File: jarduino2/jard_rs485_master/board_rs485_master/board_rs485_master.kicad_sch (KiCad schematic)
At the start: 27 parts, among them J1 POWER_12V, J2 ON_OFF, J3 POWER_OYAS_12V, J4 BUS_OYAS, J5 Leds RGB, Q1 BPC_2N2222A, Q2 BPC_IPP034N03L, Q3 BC327, U1 RtcArduino, U2 BPC_Alim3_3V, U3 BPC_ATMEGA2560_PRO, U4 BPC_Mod485

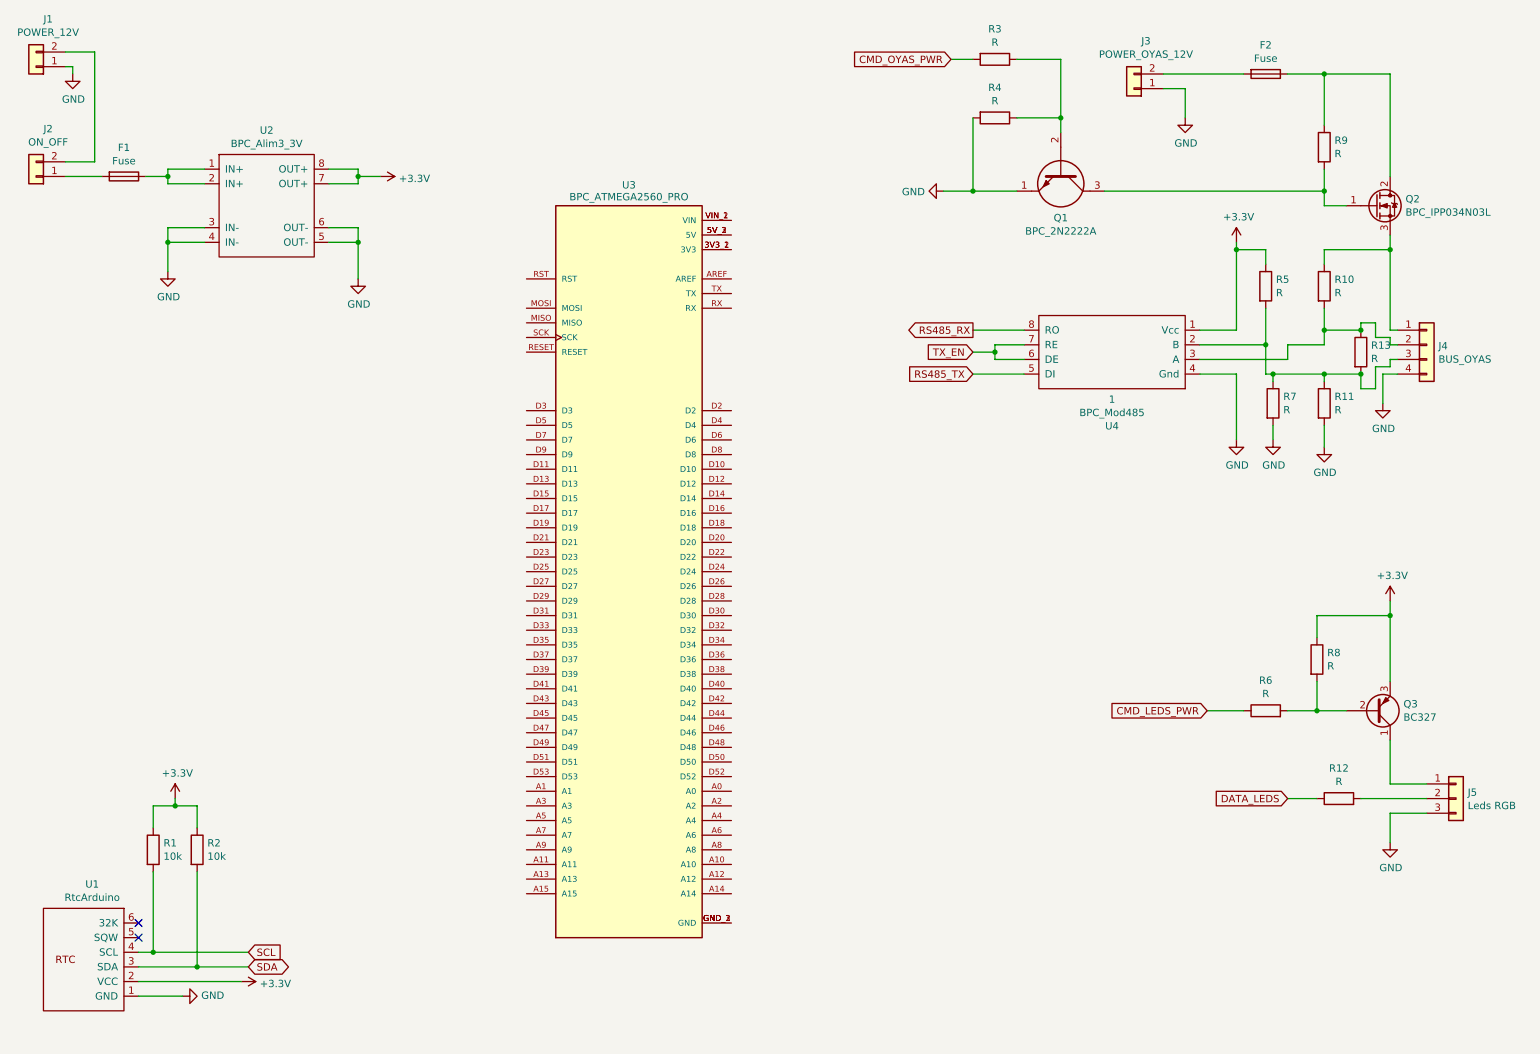
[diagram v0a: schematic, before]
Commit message: Routage carte + Ajout ESP 01 + ...
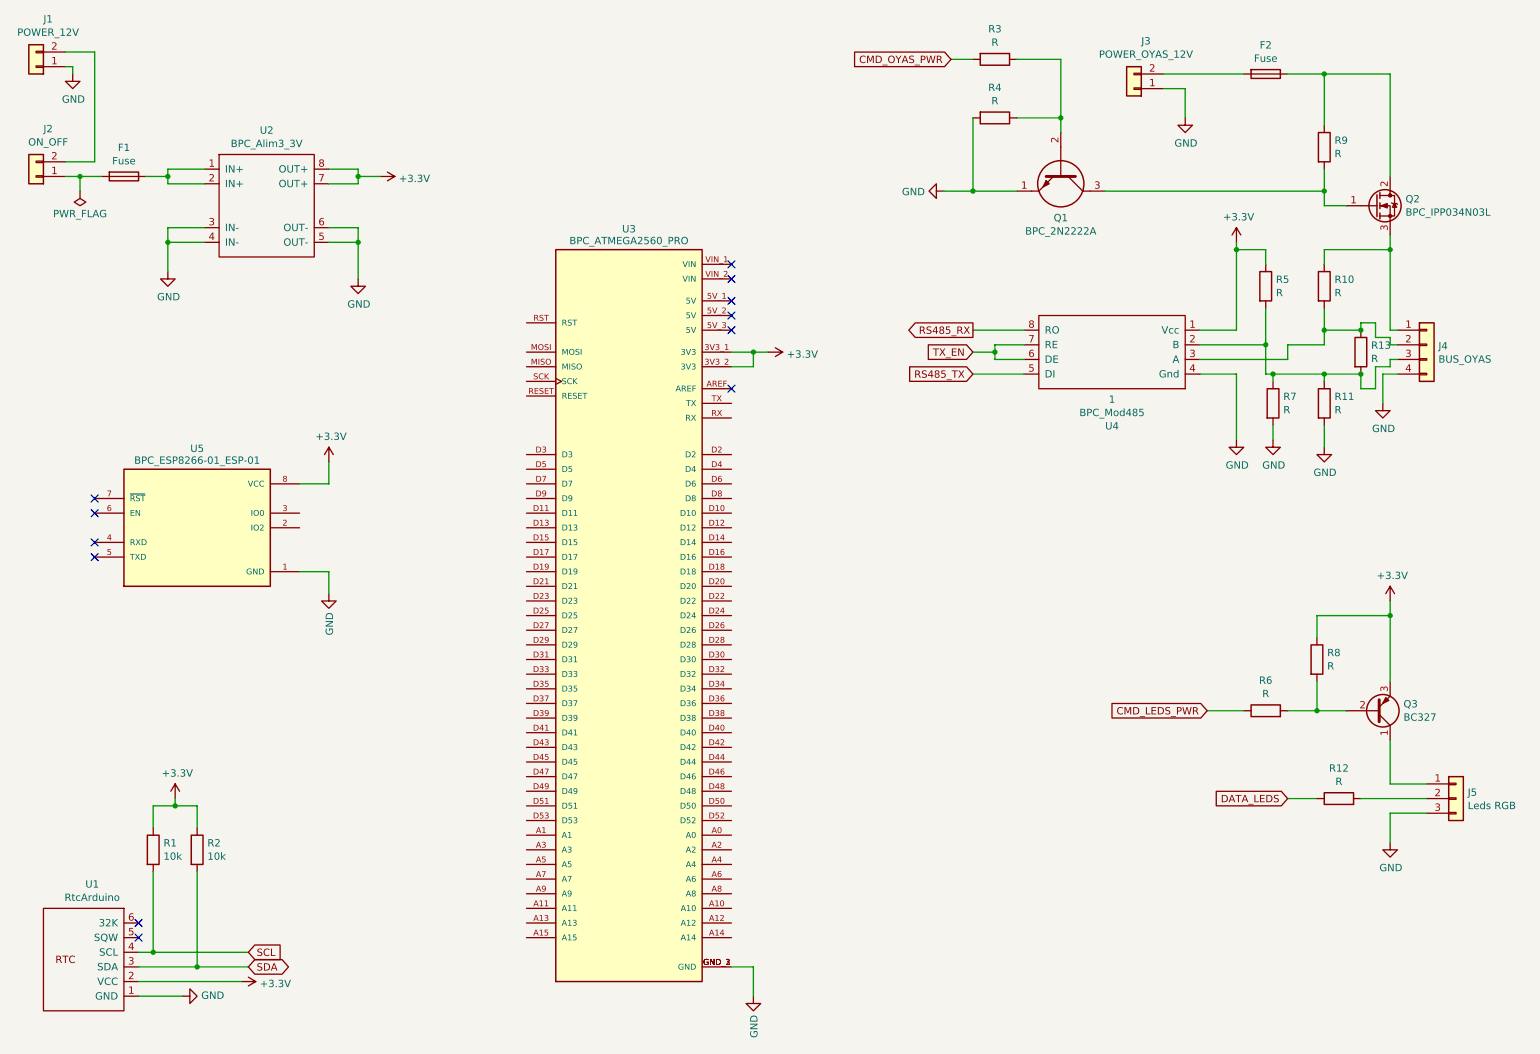
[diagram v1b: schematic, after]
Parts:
- added U5: BPC_ESP8266-01_ESP-01, bpc:BPC_XCVR_ESP8266-01_ESP-01, symbol bpc:BPC_ESP8266-01_ESP-01
- U3: footprint bpc:BPC_ATMEGA2560_PRO -> bpc:BPC_ATMEGA2560_PRO_MINI
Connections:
- net +3.3V: now also U3.3V3_1 (3V3), U3.3V3_2 (3V3), U5.8 (VCC)
- net GND: now also U3.GND_1 (GND), U3.GND_2 (GND), U3.GND_3 (GND), U5.1 (GND)
- net at U3.VIN_1 (VIN): no longer U3.VIN_2 (VIN)
- now unconnected: U3.5V_1 (5V), U3.5V_2 (5V), U3.5V_3 (5V)
- no-connect marks 2 -> 12

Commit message: Le maître des oyas devient un shield ATMEGA
- RTC
- ESP
- LEDs RGB
- Alim 5V
- RS485
- Alim 12V commutée
- Mais manque SD card....
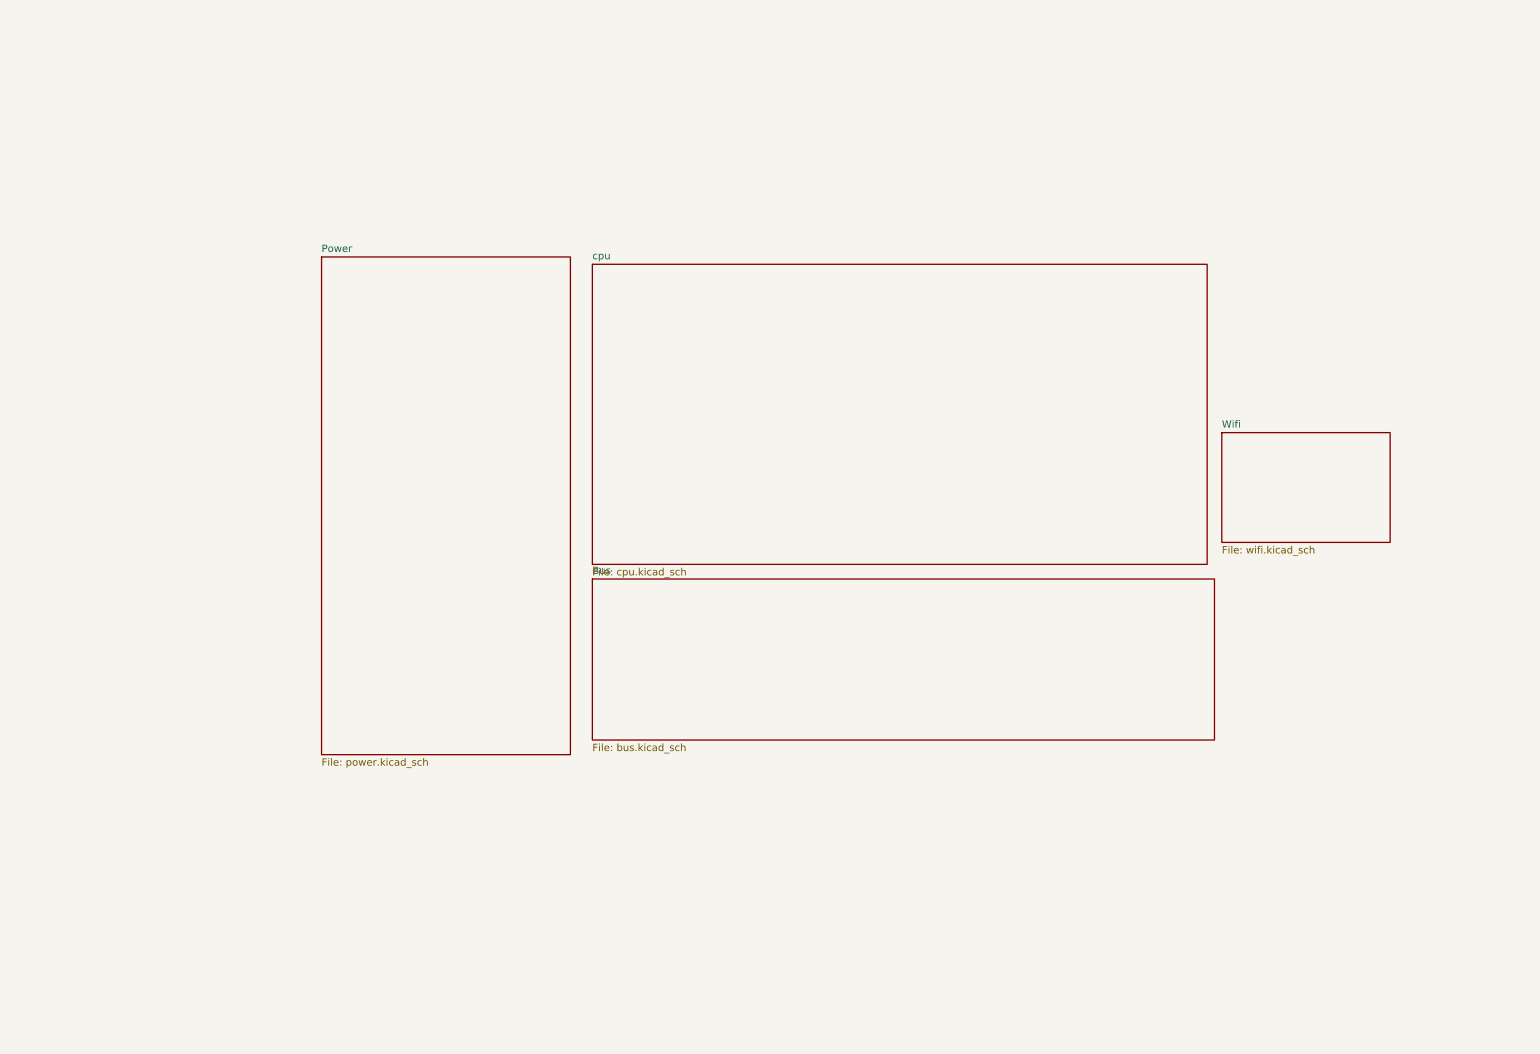
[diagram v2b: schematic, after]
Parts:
- removed F1, F2: Fuse, Fuse:Fuseholder_TR5_Littelfuse_No560_No460, symbol Device:Fuse
- removed J1: POWER_12V, TerminalBlock_Phoenix:TerminalBlock_Phoenix_MKDS-1,5-2-5.08_1x02_P5.08mm_Horizontal, symbol Connector_Generic:Conn_01x02
- removed J2: ON_OFF, TerminalBlock_Phoenix:TerminalBlock_Phoenix_MKDS-1,5-2-5.08_1x02_P5.08mm_Horizontal, symbol Connector_Generic:Conn_01x02
- removed J3: POWER_OYAS_12V, TerminalBlock_Phoenix:TerminalBlock_Phoenix_MKDS-1,5-2-5.08_1x02_P5.08mm_Horizontal, symbol Connector_Generic:Conn_01x02
- removed J4: BUS_OYAS, TerminalBlock_Phoenix:TerminalBlock_Phoenix_MKDS-1,5-4-5.08_1x04_P5.08mm_Horizontal, symbol Connector_Generic:Conn_01x04
- removed J5: Leds RGB, Connector_JST:JST_XH_B3B-XH-AM_1x03_P2.50mm_Vertical, symbol Connector_Generic:Conn_01x03
- removed Q1: BPC_2N2222A, Package_TO_SOT_THT:TO-92, symbol bpc:BPC_2N2222A
- removed Q2: BPC_IPP034N03L, Package_TO_SOT_THT:TO-220-3_Vertical, symbol bpc:BPC_IPP034N03L
- removed Q3: BC327, Package_TO_SOT_THT:TO-92_Inline, symbol Transistor_BJT:BC327
- removed R1, R2: 10k, Resistor_THT:R_Axial_DIN0204_L3.6mm_D1.6mm_P7.62mm_Horizontal, symbol Device:R
- removed R10, R11, R12, R13, R3, R4, R5, R6, R7, R8, R9: R, Resistor_THT:R_Axial_DIN0204_L3.6mm_D1.6mm_P7.62mm_Horizontal, symbol Device:R
- removed U1: RtcArduino, bpc:BPC_RtcArduino, symbol bpc:RtcArduino
- removed U2: BPC_Alim3_3V, bpc:BPC_Alim3_3V, symbol bpc:BPC_Alim3_3V
- removed U3: BPC_ATMEGA2560_PRO, bpc:BPC_ATMEGA2560_PRO_MINI, symbol bpc:BPC_ATMEGA2560_PRO
- removed U4: BPC_Mod485, bpc:BPC_Mod485, symbol bpc:BPC_Mod485
- removed U5: BPC_ESP8266-01_ESP-01, bpc:BPC_XCVR_ESP8266-01_ESP-01, symbol bpc:BPC_ESP8266-01_ESP-01
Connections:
- no-connect marks 12 -> 0
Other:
- added sheet Bus (bus.kicad_sch)
- added sheet Power (power.kicad_sch)
- added sheet Wifi (wifi.kicad_sch)
- added sheet cpu (cpu.kicad_sch)

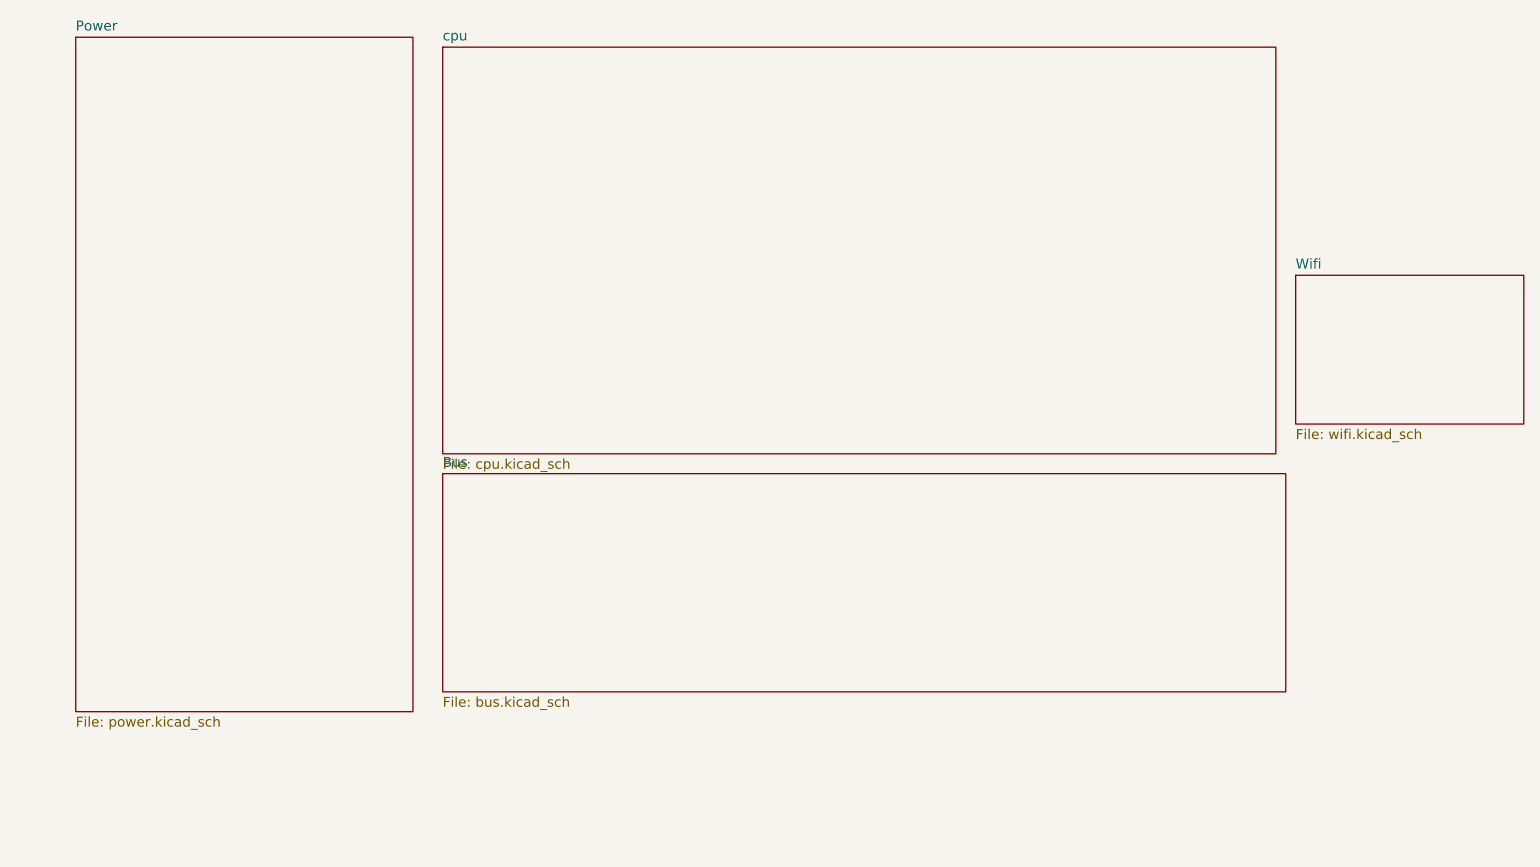
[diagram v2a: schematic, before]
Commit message: Candidate pour revue du master Oyas (avec modules en tant que shield MEGA)
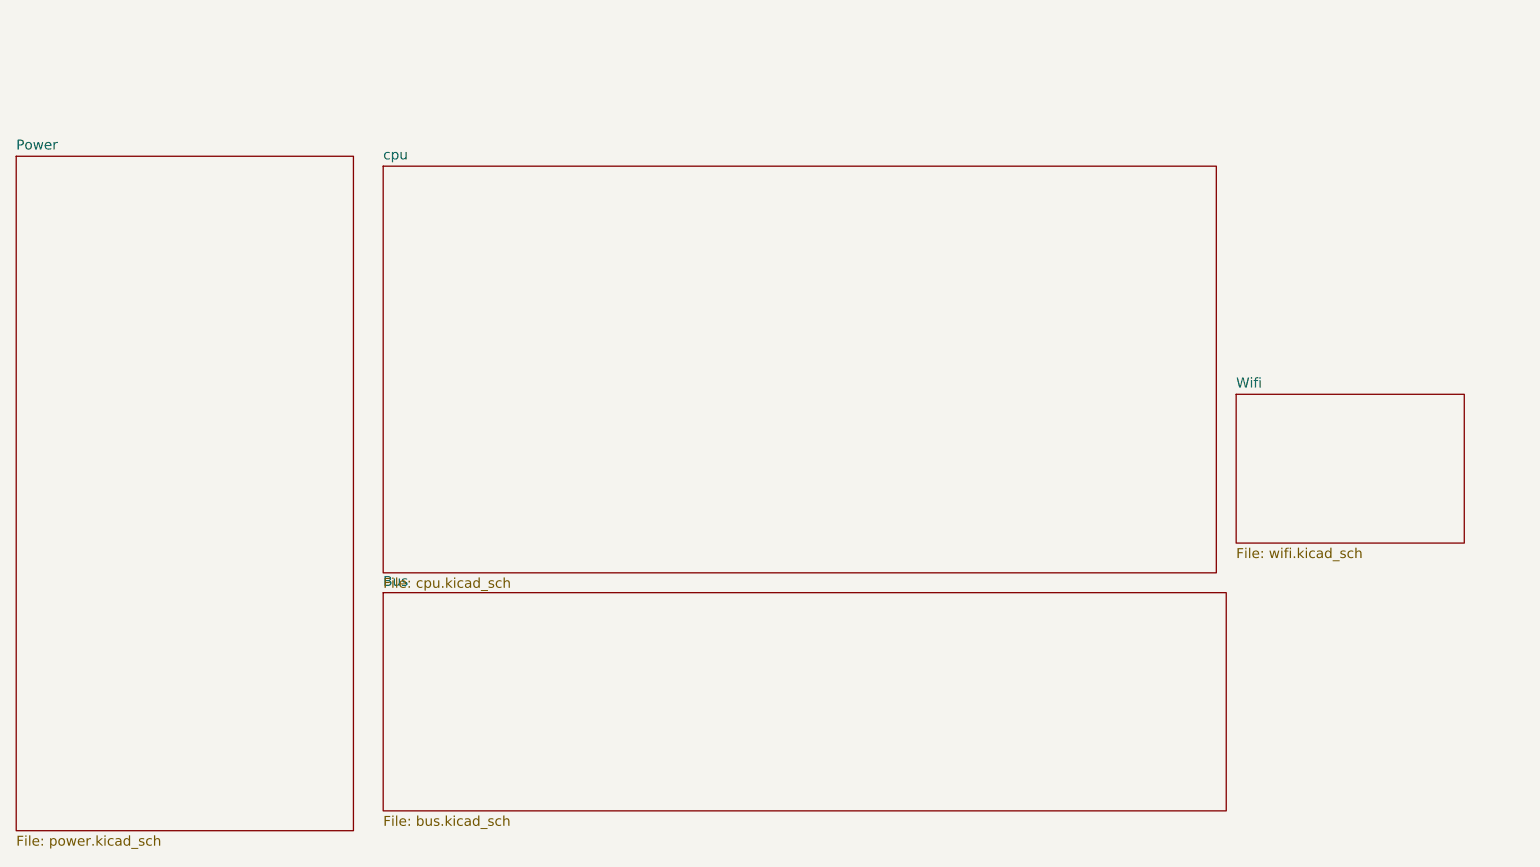
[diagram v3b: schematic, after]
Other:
- title: Carte Maître des OYAS RS485 -> Commande des OYA - Maître RS485
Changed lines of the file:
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@@
   (paper "A4")
   (title_block
-    (title "Carte Maître des OYAS RS485")
-    (date "2023-09-24")
+    (title "Commande des OYA - Maître RS485")
+    (date "2024-03-30")
     (rev "A0")
     (company "BPC")
-    (comment 3 "LEDs RGB - RTC")
+    (comment 1 "Extension Wifi (ESP01)")
+    (comment 2 "Inteface LEDs RGB - Bouton - RTC")
+    (comment 3 "Alim 12V - Sortie 12V pilotable - Bus RS485")
     (comment 4 "Maître RS485 avec alim 12 V commutée")
   )
-  (sheet (at 69.85 54.61) (size 43.18 86.36) (fields_autoplaced)
+  (sheet (at 62.23 69.85) (size 43.18 86.36) (fields_autoplaced)
     (stroke (width 0.1524) (type solid))
     (fill (color 0 0 0 0.0000))
-    (property "Sheetname" "Power" (at 69.85 53.8984 0)
+    (property "Sheetname" "Power" (at 62.23 69.1384 0)
       (effects (font (size 1.27 1.27)) (justify left bottom))
     )
-    (property "Sheetfile" "power.kicad_sch" (at 69.85 141.5546 0)
+    (property "Sheetfile" "power.kicad_sch" (at 62.23 156.7946 0)
       (effects (font (size 1.27 1.27)) (justify left top))
     )
@@
     )
   )
-  (sheet (at 226.06 85.09) (size 29.21 19.05) (fields_autoplaced)
+  (sheet (at 218.44 100.33) (size 29.21 19.05) (fields_autoplaced)
     (stroke (width 0.1524) (type solid))
     (fill (color 0 0 0 0.0000))
-    (property "Sheetname" "Wifi" (at 226.06 84.3784 0)
+    (property "Sheetname" "Wifi" (at 218.44 99.6184 0)
       (effects (font (size 1.27 1.27)) (justify left bottom))
     )
-    (property "Sheetfile" "wifi.kicad_sch" (at 226.06 104.7246 0)
+    (property "Sheetfile" "wifi.kicad_sch" (at 218.44 119.9646 0)
       (effects (font (size 1.27 1.27)) (justify left top))
     )
-    (property "Field2" "" (at 226.06 85.09 0)
+    (property "Field2" "" (at 218.44 100.33 0)
       (effects (font (size 1.27 1.27)) hide)
     )
@@
     )
   )
-  (sheet (at 116.84 110.49) (size 107.95 27.94) (fields_autoplaced)
+  (sheet (at 109.22 125.73) (size 107.95 27.94) (fields_autoplaced)
     (stroke (width 0.1524) (type solid))
     (fill (color 0 0 0 0.0000))
-    (property "Sheetname" "Bus" (at 116.84 109.7784 0)
+    (property "Sheetname" "Bus" (at 109.22 125.0184 0)
       (effects (font (size 1.27 1.27)) (justify left bottom))
     )
-    (property "Sheetfile" "bus.kicad_sch" (at 116.84 139.0146 0)
+    (property "Sheetfile" "bus.kicad_sch" (at 109.22 154.2546 0)
       (effects (font (size 1.27 1.27)) (justify left top))
     )
-    (property "Champ2" "" (at 116.84 110.49 0)
+    (property "Champ2" "" (at 109.22 125.73 0)
       (effects (font (size 1.27 1.27)) hide)
     )
@@
     )
   )
-  (sheet (at 116.84 55.88) (size 106.68 52.07) (fields_autoplaced)
+  (sheet (at 109.22 71.12) (size 106.68 52.07) (fields_autoplaced)
     (stroke (width 0.1524) (type solid))
     (fill (color 0 0 0 0.0000))
-    (property "Sheetname" "cpu" (at 116.84 55.1684 0)
+    (property "Sheetname" "cpu" (at 109.22 70.4084 0)
       (effects (font (size 1.27 1.27)) (justify left bottom))
     )
-    (property "Sheetfile" "cpu.kicad_sch" (at 116.84 108.5346 0)
+    (property "Sheetfile" "cpu.kicad_sch" (at 109.22 123.7746 0)
       (effects (font (size 1.27 1.27)) (justify left top))
     )
